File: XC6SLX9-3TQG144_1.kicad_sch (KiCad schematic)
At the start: 11 parts, among them U1 XC6SLX9-3TQG144, U2 SST25VF040B-50-4C-SAF-T

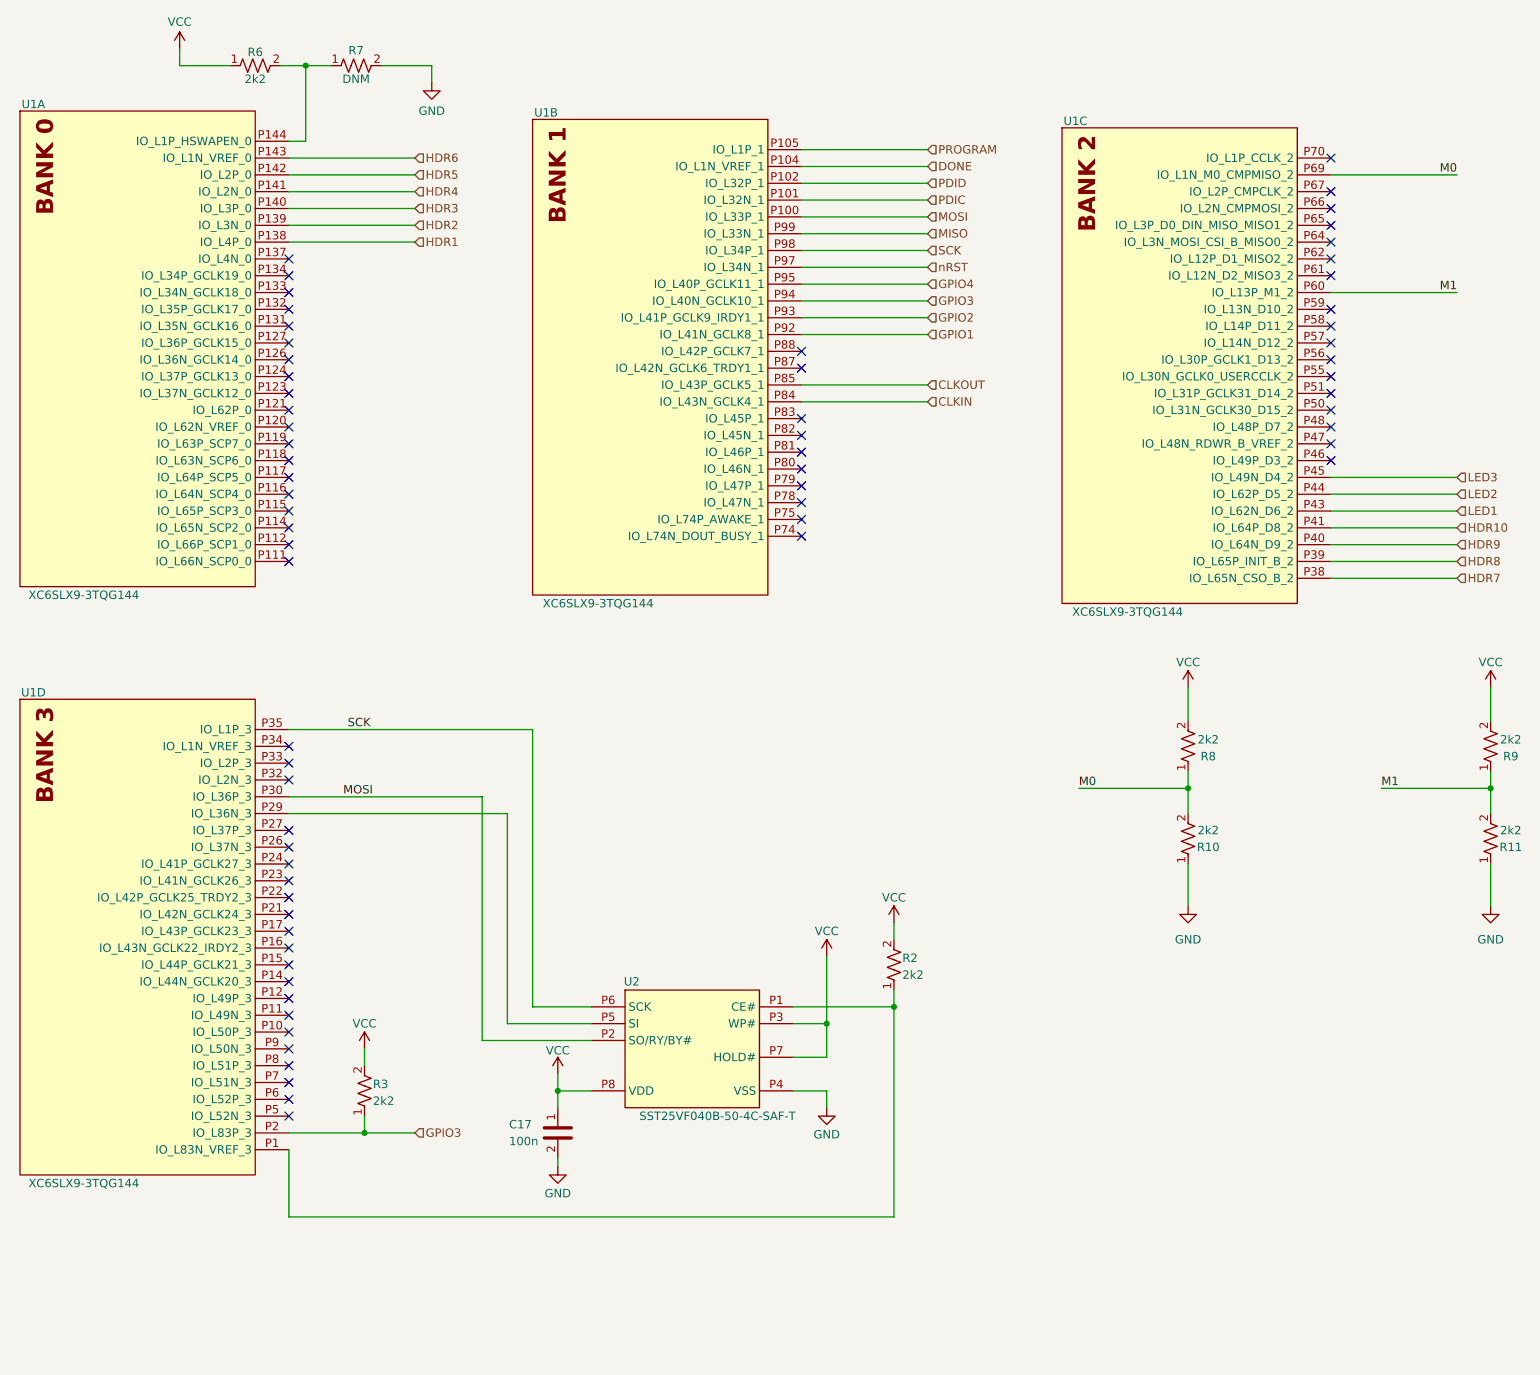
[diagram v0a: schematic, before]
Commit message: updated design - still needs vcc routing
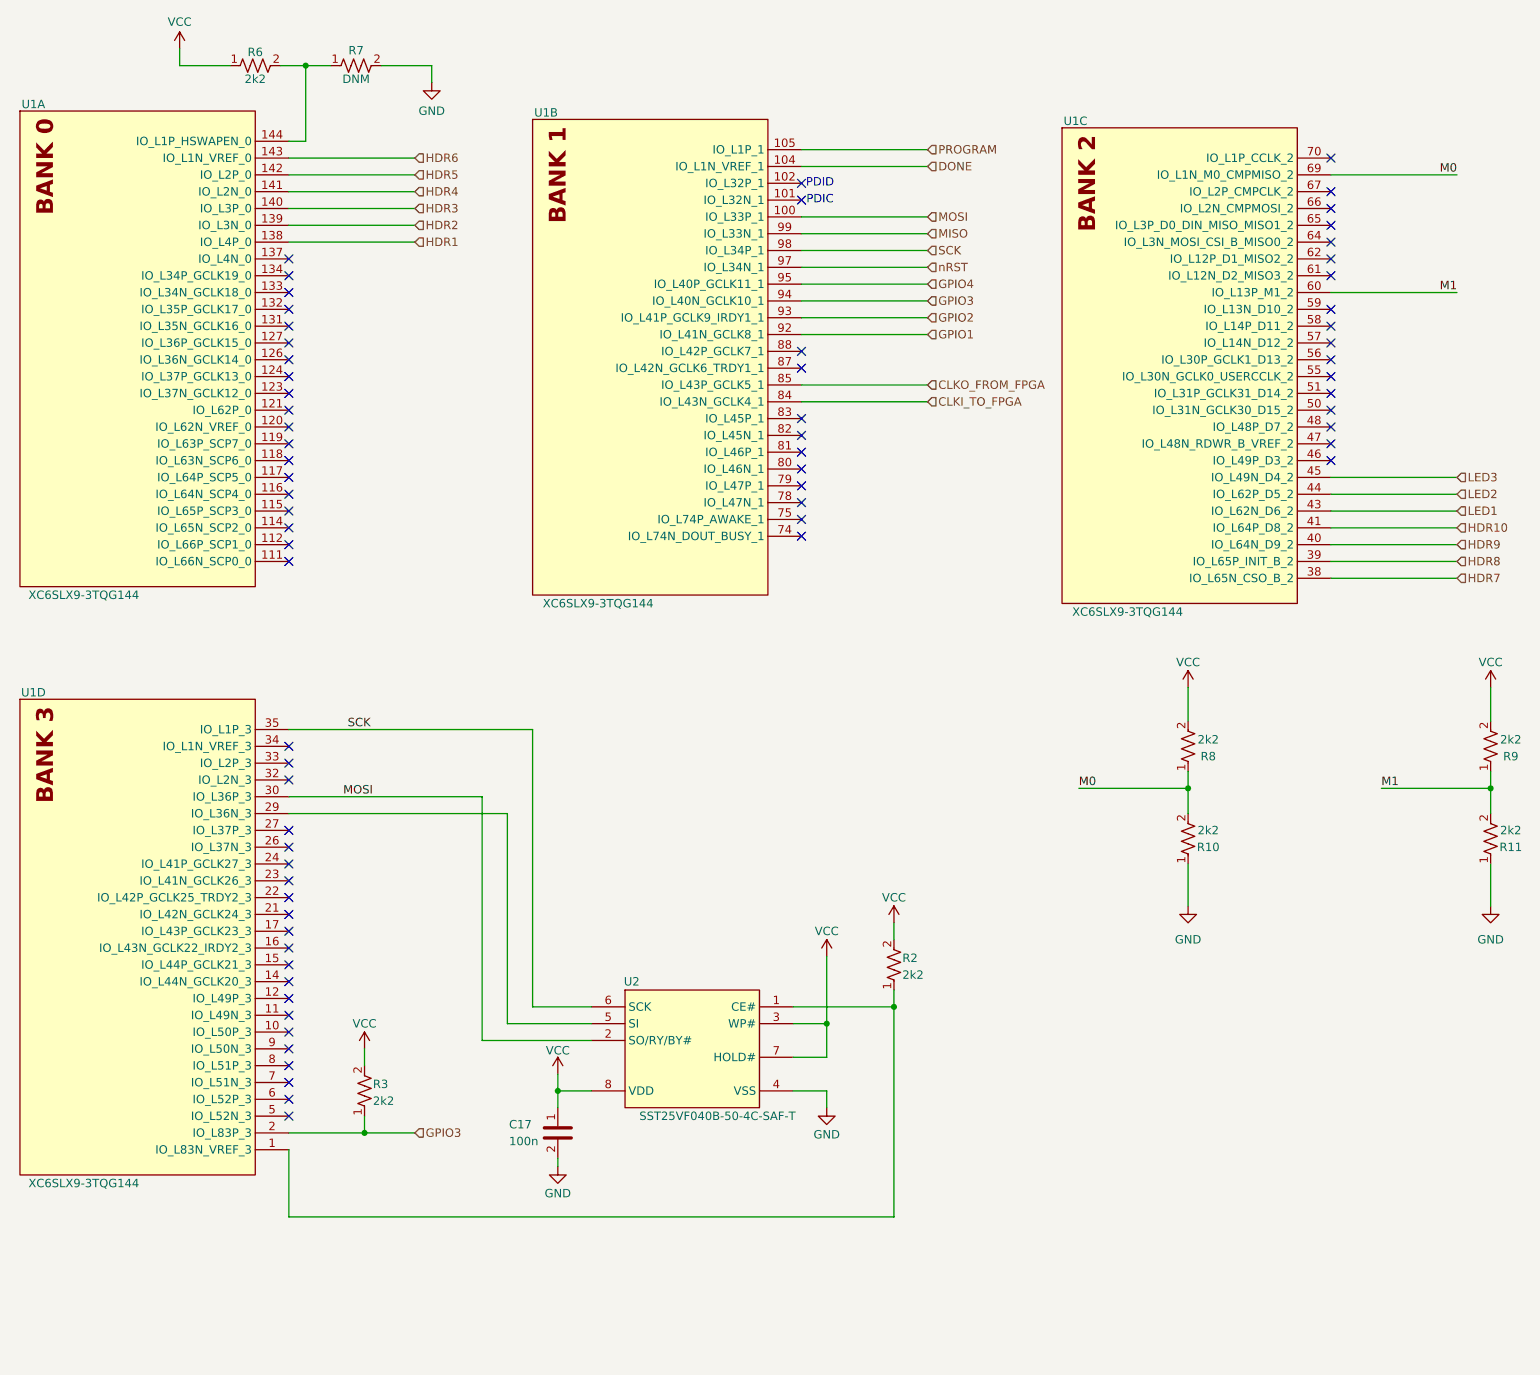
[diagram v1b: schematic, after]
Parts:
- U2: footprint Package_SO:SOIC-8_5.275x5.275mm_P1.27mm -> Package_SO:SOIC-8_3.9x4.9mm_P1.27mm
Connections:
- net DONE: now also U1.104 (IO_L1N_VREF_1); no longer U1.P104 (IO_L1N_VREF_1)
- net GND: now also U2.4 (VSS); no longer U2.P4 (VSS)
- net GPIO1: now also U1.92 (IO_L41N_GCLK8_1); no longer U1.P92 (IO_L41N_GCLK8_1)
- net GPIO2: now also U1.93 (IO_L41P_GCLK9_IRDY1_1); no longer U1.P93 (IO_L41P_GCLK9_IRDY1_1)
- net GPIO3: now also U1.2 (IO_L83P_3), U1.94 (IO_L40N_GCLK10_1); no longer U1.P2 (IO_L83P_3), U1.P94 (IO_L40N_GCLK10_1)
- net GPIO4: now also U1.95 (IO_L40P_GCLK11_1); no longer U1.P95 (IO_L40P_GCLK11_1)
- net HDR1: now also U1.138 (IO_L4P_0); no longer U1.P138 (IO_L4P_0)
- net HDR10: now also U1.41 (IO_L64P_D8_2); no longer U1.P41 (IO_L64P_D8_2)
- net HDR2: now also U1.139 (IO_L3N_0); no longer U1.P139 (IO_L3N_0)
- net HDR3: now also U1.140 (IO_L3P_0); no longer U1.P140 (IO_L3P_0)
- net HDR4: now also U1.141 (IO_L2N_0); no longer U1.P141 (IO_L2N_0)
- net HDR5: now also U1.142 (IO_L2P_0); no longer U1.P142 (IO_L2P_0)
- net HDR6: now also U1.143 (IO_L1N_VREF_0); no longer U1.P143 (IO_L1N_VREF_0)
- net HDR7: now also U1.38 (IO_L65N_CSO_B_2); no longer U1.P38 (IO_L65N_CSO_B_2)
- net HDR8: now also U1.39 (IO_L65P_INIT_B_2); no longer U1.P39 (IO_L65P_INIT_B_2)
- net HDR9: now also U1.40 (IO_L64N_D9_2); no longer U1.P40 (IO_L64N_D9_2)
- net LED1: now also U1.43 (IO_L62N_D6_2); no longer U1.P43 (IO_L62N_D6_2)
- net LED2: now also U1.44 (IO_L62P_D5_2); no longer U1.P44 (IO_L62P_D5_2)
- net LED3: now also U1.45 (IO_L49N_D4_2); no longer U1.P45 (IO_L49N_D4_2)
- net M0: now also U1.69 (IO_L1N_M0_CMPMISO_2); no longer U1.P69 (IO_L1N_M0_CMPMISO_2)
- net M1: now also U1.60 (IO_L13P_M1_2); no longer U1.P60 (IO_L13P_M1_2)
- net MISO: now also U1.99 (IO_L33N_1); no longer U1.P99 (IO_L33N_1)
- net MOSI: now also U1.100 (IO_L33P_1), U1.30 (IO_L36P_3), U2.2 (SO/RY/BY#); no longer U1.P100 (IO_L33P_1), U1.P30 (IO_L36P_3), U2.P2 (SO/RY/BY#)
- net PROGRAM: now also U1.105 (IO_L1P_1); no longer U1.P105 (IO_L1P_1)
- net SCK: now also U1.35 (IO_L1P_3), U1.98 (IO_L34P_1), U2.6 (SCK); no longer U1.P35 (IO_L1P_3), U1.P98 (IO_L34P_1), U2.P6 (SCK)
- net VCC: now also U2.3 (WP#), U2.7 (HOLD#), U2.8 (VDD); no longer U2.P3 (WP#), U2.P7 (HOLD#), U2.P8 (VDD)
- net nRST: now also U1.97 (IO_L34N_1); no longer U1.P97 (IO_L34N_1)
- net at R6.2, R7.1: now also U1.144 (IO_L1P_HSWAPEN_0); no longer U1.P144 (IO_L1P_HSWAPEN_0)
- removed net CLKIN: U1.P84 (IO_L43N_GCLK4_1)
- removed net CLKOUT: U1.P85 (IO_L43P_GCLK5_1)
- removed net PDIC: U1.P101 (IO_L32N_1)
- removed net PDID: U1.P102 (IO_L32P_1)
- new net: R2.1, U1.1 (IO_L83N_VREF_3), U2.1 (CE#)
- new net: U1.29 (IO_L36N_3), U2.5 (SI)
- new net CLKI_TO_FPGA: U1.84 (IO_L43N_GCLK4_1)
- new net CLKO_FROM_FPGA: U1.85 (IO_L43P_GCLK5_1)
- no-connect marks 67 -> 69
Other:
- note added: "PDIC"
- note added: "PDID"

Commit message: updated cw312t template
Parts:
- U2: footprint Package_SO:SOIC-8_3.9x4.9mm_P1.27mm -> Package_SO:SOIC-8_5.275x5.275mm_P1.27mm
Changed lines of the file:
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@@
 			)
 		)
-		(property "Footprint" "Package_SO:SOIC-8_3.9x4.9mm_P1.27mm"
+		(property "Footprint" "Package_SO:SOIC-8_5.275x5.275mm_P1.27mm"
 			(at 132.08 231.14 0)
 			(effects

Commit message: first draft - ready for review
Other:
- note added: "Confirm footprint/package for U2 -> matched up with the info found in data sheet but gerber of old pcb does not seem to match"
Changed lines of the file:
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@@
+		)
+	)
+	(text "Confirm footprint/package for U2 -> matched up with the info found in data sheet but gerber of old pcb does not seem to match"
+		(exclude_from_sim no)
+		(at 174.244 215.392 0)
+		(effects
+			(font
+				(size 1.27 1.27)
+			)
 		)
 	)

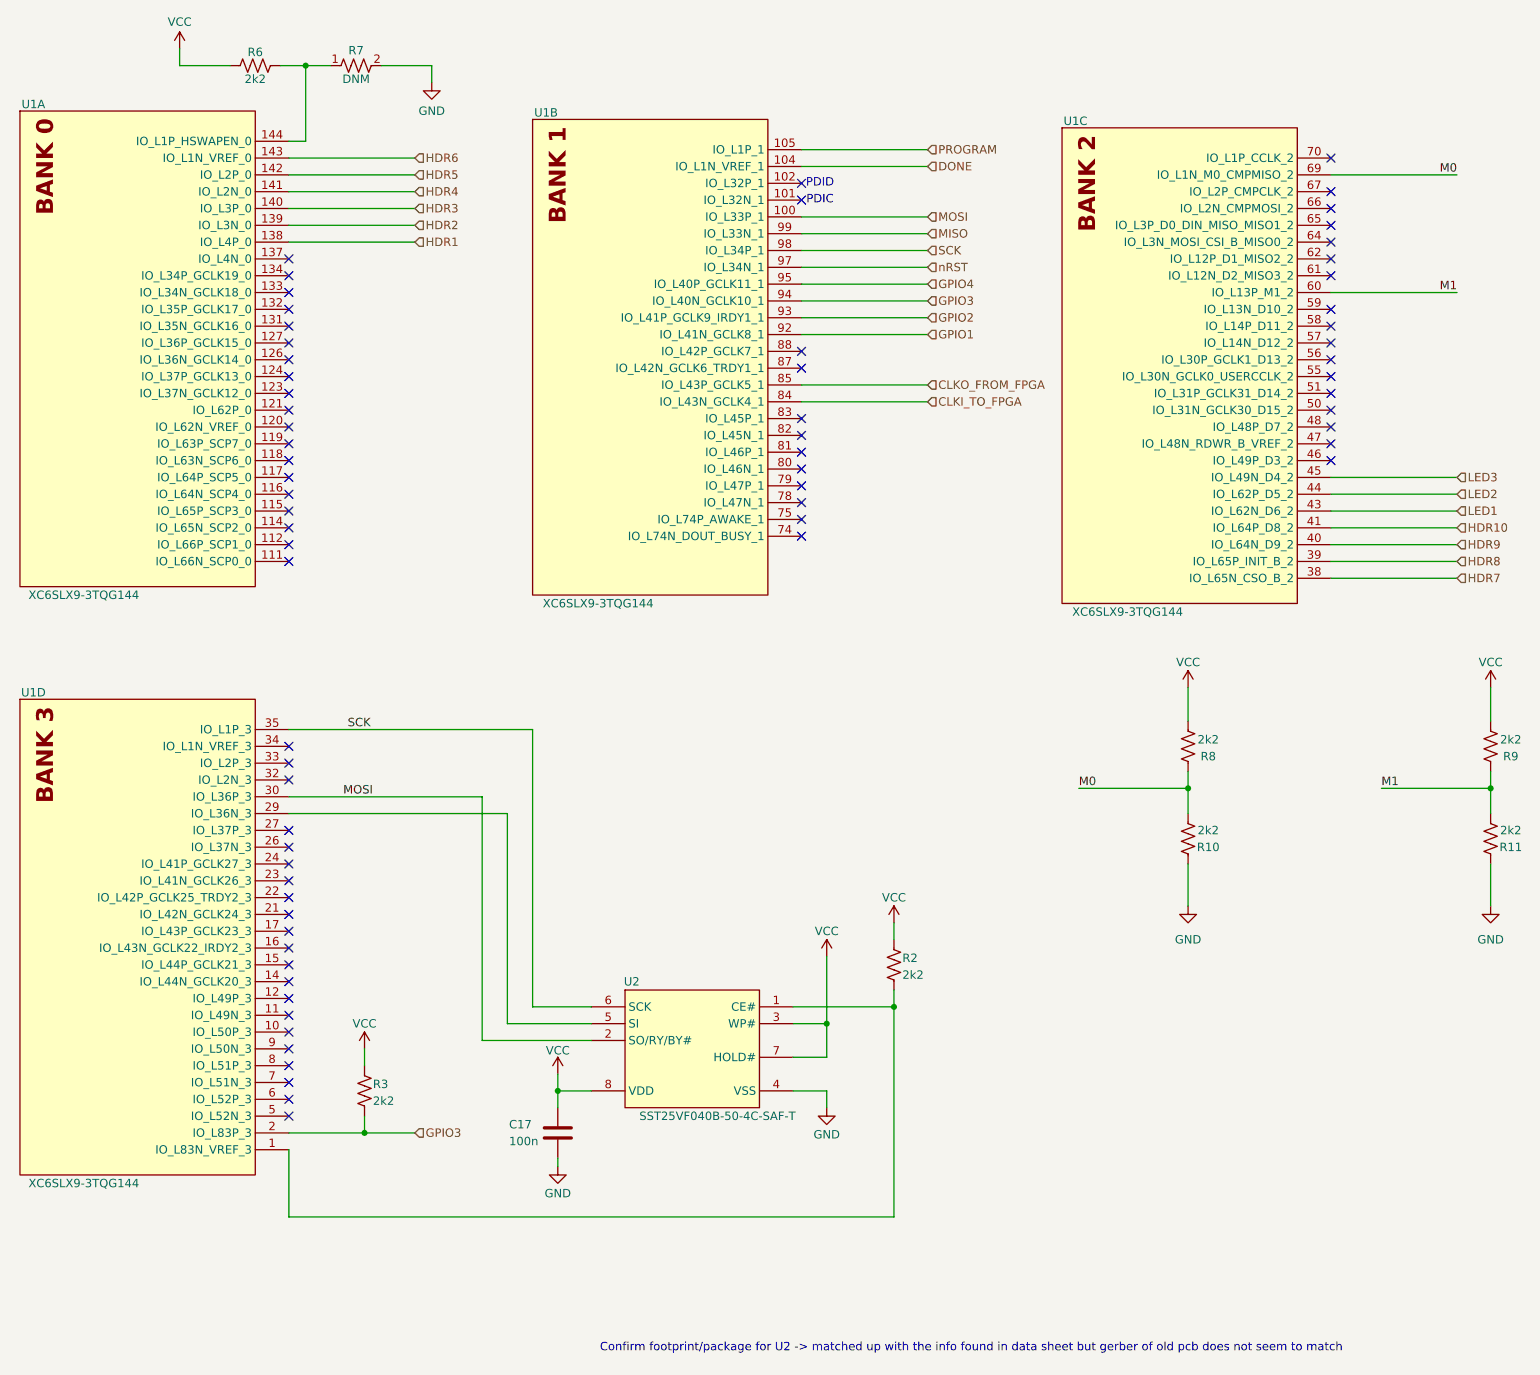
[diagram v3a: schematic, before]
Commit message: updated schematic and pcb, fixed silkscreen - Ready for review
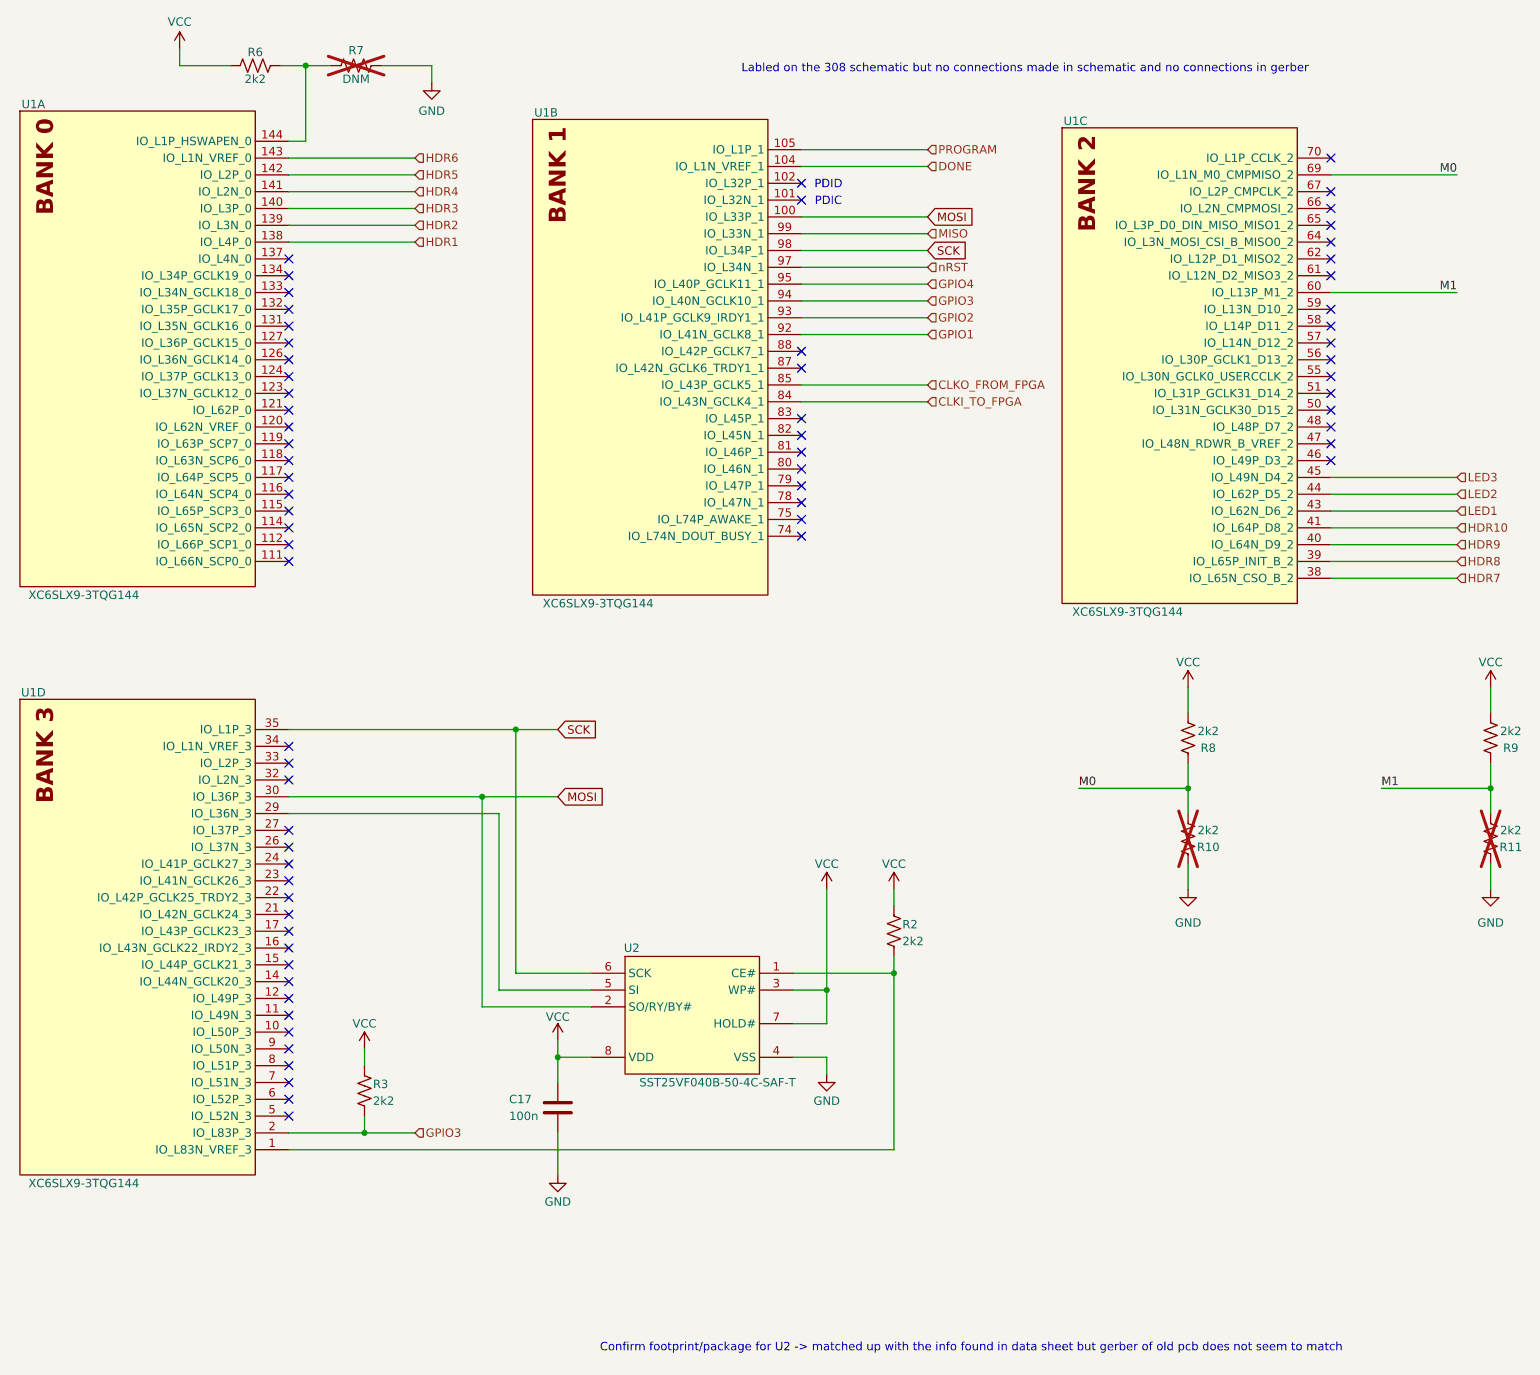
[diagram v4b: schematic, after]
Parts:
- R10, R11, R7: now not fitted
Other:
- note added: "Labled on the 308 schematic but no connections made in schematic and no connections in gerber"
- moved on the sheet: C17, R2, R7, R8, R9, U2
